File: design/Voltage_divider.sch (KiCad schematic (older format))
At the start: 2 parts

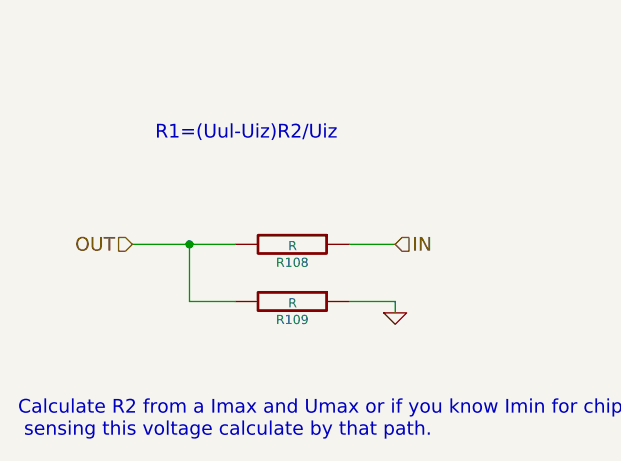
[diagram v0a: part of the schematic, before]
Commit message: Fix some ERC error, add decoupling cap to Vref+ and make some small changes to lib
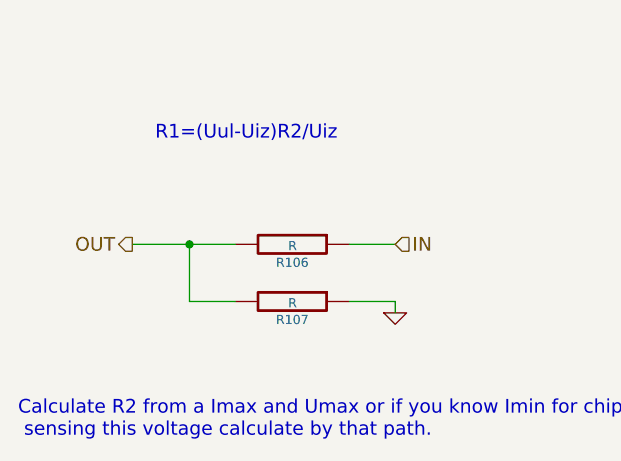
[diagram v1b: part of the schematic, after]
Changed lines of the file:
@@
 $Descr A4 11693 8268
 encoding utf-8
-Sheet 12 28
+Sheet 8 28
 Title ""
 Date ""
@@
 AR Path="/54B735D5/54E01811/54DFDF39" Ref="R106"  Part="1"
 AR Path="/54B735D5/54E0198F/54DFDF39" Ref="R108"  Part="1"
-F 0 "R108" V 5130 2950 40  0000 C CNN
+F 0 "R106" V 5130 2950 40  0000 C CNN
 F 1 "R" V 5057 2951 40  0000 C CNN
 F 2 "" V 4980 2950 30  0000 C CNN
@@
 AR Path="/54B735D5/54E01811/54DFDFD5" Ref="R107"  Part="1"
 AR Path="/54B735D5/54E0198F/54DFDFD5" Ref="R109"  Part="1"
-F 0 "R109" V 5130 3200 40  0000 C CNN
+F 0 "R107" V 5130 3200 40  0000 C CNN
 F 1 "R" V 5057 3201 40  0000 C CNN
 F 2 "" V 4980 3200 30  0000 C CNN
@@
 P 5500 3250
 AR Path="/504F83BE/54DFBF3B/54DFE01E" Ref="#PWR?"  Part="1"
-AR Path="/504F83BE/54E004A7/54DFE01E" Ref="#PWR65"  Part="1"
-AR Path="/504F83BE/54DFE437/54DFE01E" Ref="#PWR62"  Part="1"
-AR Path="/504F83BE/54DFFA62/54DFE01E" Ref="#PWR63"  Part="1"
-AR Path="/504F83BE/54DFFB5D/54DFE01E" Ref="#PWR64"  Part="1"
-AR Path="/504F83BE/54E01811/54DFE01E" Ref="#PWR66"  Part="1"
-AR Path="/504F83BE/54E0198F/54DFE01E" Ref="#PWR67"  Part="1"
-AR Path="/54B735D5/54DFE437/54DFE01E" Ref="#PWR95"  Part="1"
-AR Path="/54B735D5/54DFFA62/54DFE01E" Ref="#PWR96"  Part="1"
-AR Path="/54B735D5/54DFFB5D/54DFE01E" Ref="#PWR97"  Part="1"
-AR Path="/54B735D5/54E004A7/54DFE01E" Ref="#PWR98"  Part="1"
-AR Path="/54B735D5/54E01811/54DFE01E" Ref="#PWR99"  Part="1"
-AR Path="/54B735D5/54E0198F/54DFE01E" Ref="#PWR100"  Part="1"
-F 0 "#PWR100" H 5500 3250 30  0001 C CNN
+AR Path="/504F83BE/54E004A7/54DFE01E" Ref="#PWR068"  Part="1"
+AR Path="/504F83BE/54DFE437/54DFE01E" Ref="#PWR065"  Part="1"
+AR Path="/504F83BE/54DFFA62/54DFE01E" Ref="#PWR066"  Part="1"
+AR Path="/504F83BE/54DFFB5D/54DFE01E" Ref="#PWR067"  Part="1"
+AR Path="/504F83BE/54E01811/54DFE01E" Ref="#PWR073"  Part="1"
+AR Path="/504F83BE/54E0198F/54DFE01E" Ref="#PWR069"  Part="1"
+AR Path="/54B735D5/54DFE437/54DFE01E" Ref="#PWR0101"  Part="1"
+AR Path="/54B735D5/54DFFA62/54DFE01E" Ref="#PWR0102"  Part="1"
+AR Path="/54B735D5/54DFFB5D/54DFE01E" Ref="#PWR0103"  Part="1"
+AR Path="/54B735D5/54E004A7/54DFE01E" Ref="#PWR0104"  Part="1"
+AR Path="/54B735D5/54E01811/54DFE01E" Ref="#PWR0109"  Part="1"
+AR Path="/54B735D5/54E0198F/54DFE01E" Ref="#PWR0105"  Part="1"
+F 0 "#PWR0109" H 5500 3250 30  0001 C CNN
 F 1 "GND" H 5500 3180 30  0001 C CNN
 F 2 "" H 5500 3250 60  0000 C CNN
@@
 Text HLabel 5500 2950 2    60   Input ~ 0
 IN
-Text HLabel 4350 2950 0    60   Input ~ 0
+Text HLabel 4350 2950 0    60   Output ~ 0
 OUT
 Text Notes 4450 2500 0    60   ~ 0
